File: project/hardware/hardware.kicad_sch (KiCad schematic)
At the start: 102 parts, among them IC1 TAS5760LDAPR, J1 798-DM3D-SF, J2 Conn_01x04, J3 Conn_01x04, J4 USB-C, SW1 SW_Push, SW2 SW_Push, SW3 SW_Push, SW5 SW_Push, U1 TPS563200, U2 ESP32-S3, U3 USBLC6-2SC6, Y1 ECS-400-10-36B2-CKM-TR, Y2 ABS07-166-32.768KHZ-T

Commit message: faltando o plano de terra da antena
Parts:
- added J5, J6: Conn_01x02_Socket, Connector_PinSocket_2.54mm:PinSocket_2x01_P2.54mm_Vertical_SMD, symbol Connector:Conn_01x02_Socket
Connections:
- net +12V: now also J5.1 (Pin_1)
- net +8V: now also J6.1 (Pin_1)
- net BT_L: now also U2.27 (GPIO21); no longer U2.19 (GPIO14)
- net BT_R: now also U2.19 (GPIO14); no longer U2.27 (GPIO21)
- net GND: no longer ANT1.2, C1.1, C10.2, C12.2, C16.1, C2.1, C22.1, C23.1, C24.1, C3.2, C30.1, C35.1, C36.2, C37.1, C38.1, C39.1, C4.1, C40.1, C41.2, C42.1, C43.1, C44.2, C45.1, C5.2, C7.1, C9.1, D1.1 (A), IC1.18 (DGND), IC1.22 (PGND_1), IC1.27 (PGND_2), IC1.31 (GGND), IC1.33 (EP), J1.11 (SHIELD), J2.4 (Pin_4), J3.4 (Pin_4), R10.1, R16.2, R20.2, SW3.1, SW5.1, U2.51 (GPIO45), U2.52 (GPIO46), U2.57 (GND), Y1.2, Y1.4
- net PWR_GND renamed GND_E
- net GND_E: now also ANT1.2, C1.1, C10.2, C12.2, C16.1, C2.1, C22.1, C23.1, C24.1, C3.2, C4.1, C45.1, C5.2, C7.1, C9.1, D1.1 (A), J1.11 (SHIELD), J2.4 (Pin_4), J3.4 (Pin_4), R10.1, R16.2, R20.2, SW3.1, SW5.1, U2.51 (GPIO45), U2.52 (GPIO46), U2.57 (GND), Y1.2, Y1.4, J5.2 (Pin_2)
- new net GND_ANALOG: C30.1, C35.1, C36.2, C37.1, C38.1, C39.1, C40.1, C41.2, C42.1, C43.1, C44.2, IC1.18 (DGND), IC1.22 (PGND_1), IC1.27 (PGND_2), IC1.31 (GGND), IC1.33 (EP), J6.2 (Pin_2)

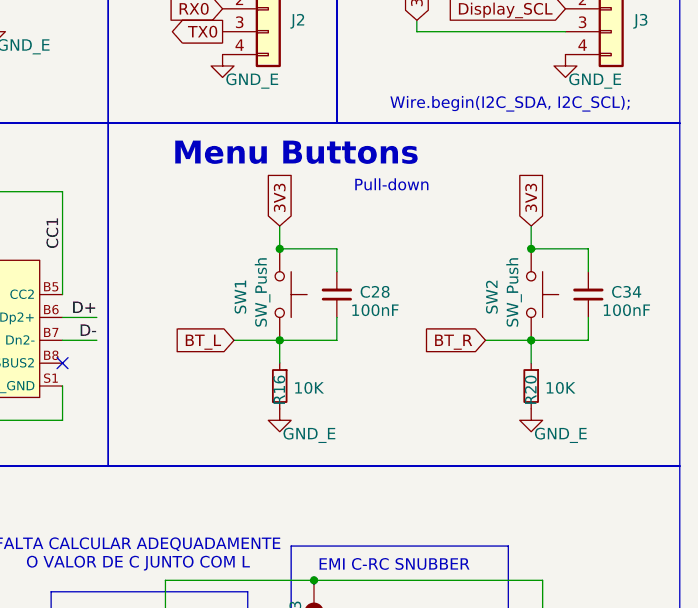
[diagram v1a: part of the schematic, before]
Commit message: updating button topology on schematic
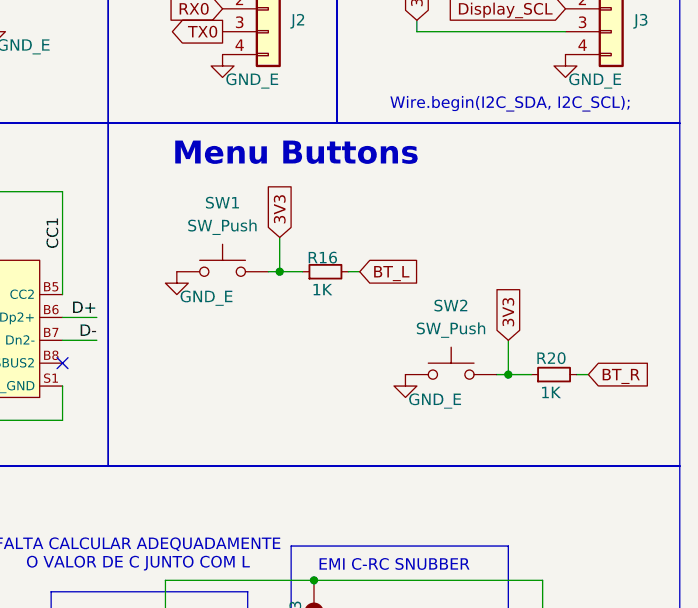
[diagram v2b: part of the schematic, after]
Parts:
- removed C28, C34: 100nF, Capacitor_SMD:C_0402_1005Metric, symbol Device:C_Small
- R16, R20: value 10K -> 1K; footprint Resistor_SMD:R_0201_0603Metric_Pad0.64x0.40mm_HandSolder -> Resistor_SMD:R_0402_1005Metric
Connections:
- net 3V3: now also R16.1, R20.1, SW1.2, SW2.2; no longer SW1.1, SW2.1
- net BT_L: now also R16.2; no longer R16.1, SW1.2
- net BT_R: now also R20.2; no longer R20.1, SW2.2
- net GND_E: now also SW1.1, SW2.1; no longer R16.2, R20.2
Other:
- note removed: "Pull-down"
